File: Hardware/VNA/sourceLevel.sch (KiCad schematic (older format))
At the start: 23 parts, among them U5 AD8319, U6 PE43711, U7 TRF37A75

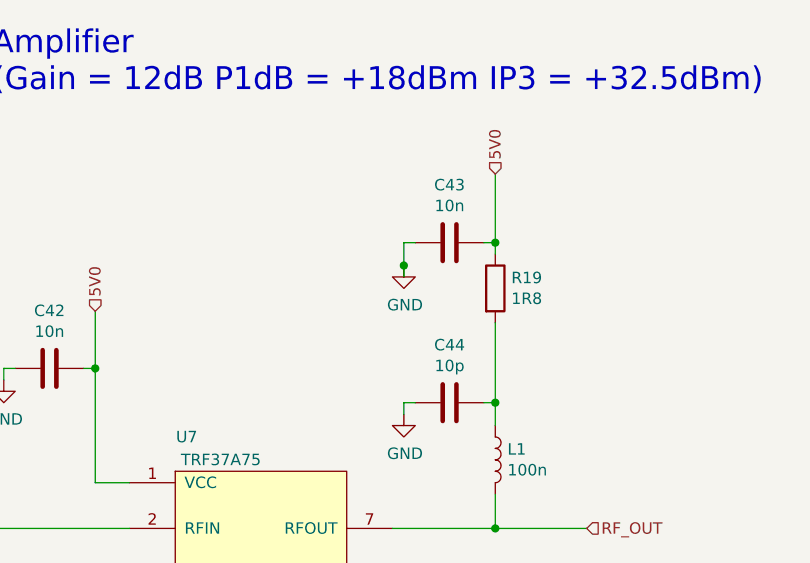
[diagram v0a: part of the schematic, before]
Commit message: added footprints and 3d models
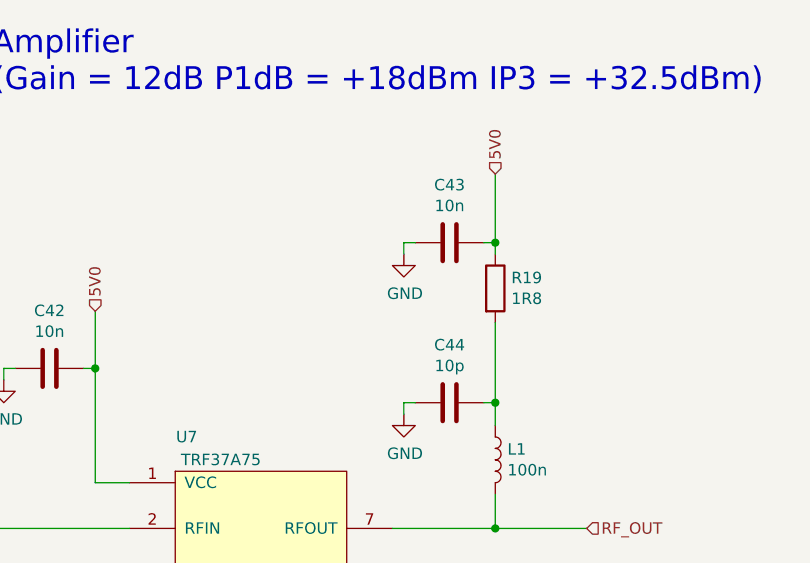
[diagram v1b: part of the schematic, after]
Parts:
- R17, R18: footprint (none) -> Resistor_SMD:R_0603_1608Metric
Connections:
- wire segments 110 -> 109
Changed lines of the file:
@@
 Connection ~ 6500 3800
 $Comp
-L power:GND #PWR045
+L power:GND #PWR044
 U 1 1 5C86EFC4
 P 6800 3850
-F 0 "#PWR045" H 6800 3600 50  0001 C CNN
+F 0 "#PWR044" H 6800 3600 50  0001 C CNN
 F 1 "GND" H 6805 3677 50  0000 C CNN
 F 2 "" H 6800 3850 50  0001 C CNN
@@
 F 0 "R17" H 5470 3446 50  0000 L CNN
 F 1 "0R" H 5470 3355 50  0000 L CNN
-F 2 "" V 5330 3400 50  0001 C CNN
+F 2 "Resistor_SMD:R_0603_1608Metric" V 5330 3400 50  0001 C CNN
 F 3 "~" H 5400 3400 50  0001 C CNN
 	1    5400 3400
@@
 F 0 "R18" H 5470 3846 50  0000 L CNN
 F 1 "DNP" H 5470 3755 50  0000 L CNN
-F 2 "" V 5330 3800 50  0001 C CNN
+F 2 "Resistor_SMD:R_0603_1608Metric" V 5330 3800 50  0001 C CNN
 F 3 "~" H 5400 3800 50  0001 C CNN
 	1    5400 3800
@@
 	5400 3250 5400 3200
 $Comp
-L power:GND #PWR043
+L power:GND #PWR042
 U 1 1 5CB1FC94
 P 5400 4000
-F 0 "#PWR043" H 5400 3750 50  0001 C CNN
+F 0 "#PWR042" H 5400 3750 50  0001 C CNN
 F 1 "GND" H 5405 3827 50  0000 C CNN
 F 2 "" H 5400 4000 50  0001 C CNN
@@
 	7600 1350 7600 1650
 $Comp
+L power:GND #PWR045
+U 1 1 5C8784A2
+P 7200 1700
+F 0 "#PWR045" H 7200 1450 50  0001 C CNN
+F 1 "GND" H 7205 1527 50  0000 C CNN
+F 2 "" H 7200 1700 50  0001 C CNN
+F 3 "" H 7200 1700 50  0001 C CNN
+	1    7200 1700
+	1    0    0    -1
+$EndComp
+$Comp
 L power:GND #PWR046
-U 1 1 5C8784A2
-P 7200 1750
-F 0 "#PWR046" H 7200 1500 50  0001 C CNN
-F 1 "GND" H 7205 1577 50  0000 C CNN
-F 2 "" H 7200 1750 50  0001 C CNN
-F 3 "" H 7200 1750 50  0001 C CNN
-	1    7200 1750
-	1    0    0    -1
-$EndComp
-$Comp
-L power:GND #PWR047
 U 1 1 5C87587D
 P 7200 2400
-F 0 "#PWR047" H 7200 2150 50  0001 C CNN
+F 0 "#PWR046" H 7200 2150 50  0001 C CNN
 F 1 "GND" H 7205 2227 50  0000 C CNN
 F 2 "" H 7200 2400 50  0001 C CNN
@@
 $EndComp
 Wire Wire Line
-	7200 1650 7200 1750
-Wire Wire Line
 	5450 2200 5450 2250
 $Comp
-L power:GND #PWR044
+L power:GND #PWR043
 U 1 1 5CCF0441
 P 5450 2250
-F 0 "#PWR044" H 5450 2000 50  0001 C CNN
+F 0 "#PWR043" H 5450 2000 50  0001 C CNN
 F 1 "GND" H 5455 2077 50  0000 C CNN
 F 2 "" H 5450 2250 50  0001 C CNN
@@
 Wire Wire Line
 	5150 5700 5150 5750
-Connection ~ 7200 1750
-Wire Wire Line
-	7200 1750 7200 1800
 Text HLabel 2450 5200 0    50   Input ~ 0
 RF_PWR_IN
@@
 	7250 3200 7150 3200
 $Comp
-L power:GND #PWR048
+L power:GND #PWR047
 U 1 1 5C86ED9F
 P 7250 3300
-F 0 "#PWR048" H 7250 3050 50  0001 C CNN
+F 0 "#PWR047" H 7250 3050 50  0001 C CNN
 F 1 "GND" H 7255 3127 50  0000 C CNN
 F 2 "" H 7250 3300 50  0001 C CNN
@@
 Text HLabel 5400 3200 1    50   Input ~ 0
 3V3A
+Wire Wire Line
+	7200 1650 7200 1700
 $EndSCHEMATC

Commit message: prelim schematic capture complete
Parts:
- renumbered C34 to C36, C35 to C37, C36 to C38, C37 to C39, C38 to C40, C39 to C41, C40 to C42, C41 to C43, C42 to C44, C43 to C45, C44 to C46, R12 to R19, R13 to R20, R14 to R21, R15 to R22, R16 to R23, R17 to R24, R18 to R25, R19 to R26, U5 to U7, U6 to U8, U7 to U9

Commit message: all 3d models created, prelim bom generated
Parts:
- added TP16: TP, TestPoint:TestPoint_Pad_D1.0mm, symbol Connector:TestPoint
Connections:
- wire segments 109 -> 114
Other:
- moved on the sheet: C38, C39
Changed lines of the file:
@@
 	1    0    0    -1
 $EndComp
-Text Label 4700 3350 2    50   ~ 6
+Text Label 4700 3350 2    50   ~ 0
 nP_S
-Text Label 4700 3500 2    50   ~ 6
-SI
-Text Label 4700 3700 2    50   ~ 6
-LE
-Text Label 4700 3600 2    50   ~ 6
-CLK
 Wire Wire Line
 	4400 3500 4700 3500
@@
 L Device:C C39
 U 1 1 5CC58ACB
-P 3750 2300
-F 0 "C39" V 3700 2200 50  0000 C CNN
-F 1 "100p" V 3900 2300 50  0000 C CNN
-F 2 "Capacitor_SMD:C_0402_1005Metric" H 3788 2150 50  0001 C CNN
-F 3 "~" H 3750 2300 50  0001 C CNN
-	1    3750 2300
+P 3900 2300
+F 0 "C39" V 3850 2150 50  0000 C CNN
+F 1 "100p" V 4050 2300 50  0000 C CNN
+F 2 "Capacitor_SMD:C_0402_1005Metric" H 3938 2150 50  0001 C CNN
+F 3 "~" H 3900 2300 50  0001 C CNN
+	1    3900 2300
 	0    1    1    0
 $EndComp
@@
 L Device:C C38
 U 1 1 5C364B92
-P 3750 1950
-F 0 "C38" V 3700 1850 50  0000 C CNN
-F 1 "100n" V 3900 1950 50  0000 C CNN
-F 2 "Capacitor_SMD:C_0402_1005Metric" H 3788 1800 50  0001 C CNN
-F 3 "~" H 3750 1950 50  0001 C CNN
-	1    3750 1950
-	0    1    1    0
-$EndComp
-Wire Wire Line
-	3600 1750 3600 1950
+P 3900 1950
+F 0 "C38" V 3850 1800 50  0000 C CNN
+F 1 "100n" V 4050 1950 50  0000 C CNN
+F 2 "Capacitor_SMD:C_0402_1005Metric" H 3938 1800 50  0001 C CNN
+F 3 "~" H 3900 1950 50  0001 C CNN
+	1    3900 1950
+	0    1    1    0
+$EndComp
 $Comp
 L power:GND #PWR058
 U 1 1 5C36FE30
-P 3900 2400
-F 0 "#PWR058" H 3900 2150 50  0001 C CNN
-F 1 "GND" H 3905 2227 50  0000 C CNN
-F 2 "" H 3900 2400 50  0001 C CNN
-F 3 "" H 3900 2400 50  0001 C CNN
-	1    3900 2400
-	1    0    0    -1
-$EndComp
-Connection ~ 3600 1950
-Wire Wire Line
-	3900 2300 3900 2400
-Connection ~ 3600 2300
-Wire Wire Line
-	3600 1950 3600 2300
-Wire Wire Line
-	3900 1950 3900 2300
-Connection ~ 3900 2300
-Wire Wire Line
-	3600 2300 3600 2550
-Text Notes 2750 850  0    100  ~ 6
+P 4050 2400
+F 0 "#PWR058" H 4050 2150 50  0001 C CNN
+F 1 "GND" H 4055 2227 50  0000 C CNN
+F 2 "" H 4050 2400 50  0001 C CNN
+F 3 "" H 4050 2400 50  0001 C CNN
+	1    4050 2400
+	1    0    0    -1
+$EndComp
+Wire Wire Line
+	4050 2300 4050 2400
+Wire Wire Line
+	4050 1950 4050 2300
+Connection ~ 4050 2300
+Text Notes 2750 850  0    100  ~ 0
 Programmable Attenuator
 Wire Wire Line
@@
 Wire Wire Line
 	5400 3600 5400 3650
-Text HLabel 2500 2900 0    50   Input ~ 6
+Text HLabel 2500 2900 0    50   Input ~ 0
 RF_IN
-Text HLabel 8000 2900 2    50   Input ~ 6
+Text HLabel 8000 2900 2    50   Input ~ 0
 RF_OUT
-Text HLabel 4700 3500 2    50   Input ~ 6
+Text HLabel 4700 3500 2    50   Input ~ 0
 SI
 Wire Wire Line
@@
 Connection ~ 4350 6100
 Wire Wire Line
-	4850 6100 5250 6100
-Text Notes 2900 4900 0    100  ~ 6
+	4850 6100 5050 6100
+Text Notes 2900 4900 0    100  ~ 0
 Power Detector\n
 $Comp
@@
 Wire Wire Line
 	5000 5700 5150 5700
-Text HLabel 4700 3600 2    50   Input ~ 6
+Text HLabel 4700 3600 2    50   Input ~ 0
 CLK
-Text HLabel 4700 3700 2    50   Input ~ 6
+Text HLabel 4700 3700 2    50   Input ~ 0
 LE
-Text Notes 5400 1000 0    100  ~ 6
+Text Notes 5400 1000 0    100  ~ 0
 Amplifier \n(Gain = 12dB P1dB = +18dBm IP3 = +32.5dBm)
 Wire Wire Line
@@
 Wire Wire Line
 	5150 5700 5150 5750
-Text HLabel 2450 5200 0    50   Input ~ 6
+Text HLabel 2450 5200 0    50   Input ~ 0
 RF_PWR_IN
-Text HLabel 5250 6100 2    50   Output ~ 6
+Text HLabel 5250 6100 2    50   Output ~ 0
 PWR_LEVEL
-Text HLabel 3600 1750 1    50   Input ~ 6
+Text HLabel 3600 1750 1    50   Input ~ 0
 3V3A
-Text HLabel 5850 1950 1    50   Input ~ 6
+Text HLabel 5850 1950 1    50   Input ~ 0
 5V0
-Text HLabel 7600 1350 1    50   Input ~ 6
+Text HLabel 7600 1350 1    50   Input ~ 0
 5V0
 Wire Wire Line
@@
 Wire Wire Line
 	7250 3300 7250 3200
-Text HLabel 6000 3200 0    50   Input ~ 6
+Text HLabel 6000 3200 0    50   Input ~ 0
 PWRDN
-Text HLabel 4650 5350 1    50   Input ~ 6
+Text HLabel 4650 5350 1    50   Input ~ 0
 3V3A
-Text HLabel 5400 3200 1    50   Input ~ 6
+Text HLabel 5400 3200 1    50   Input ~ 0
 3V3A
 Wire Wire Line
 	7200 1650 7200 1700
+$Comp
+L Connector:TestPoint TP16
+U 1 1 5CECA150
+P 5150 6300
+F 0 "TP16" V 5104 6488 50  0000 L CNN
+F 1 "TP" V 5195 6488 50  0000 L CNN
+F 2 "TestPoint:TestPoint_Pad_D1.0mm" H 5350 6300 50  0001 C CNN
+F 3 "~" H 5350 6300 50  0001 C CNN
+	1    5150 6300
+	0    1    1    0
+$EndComp
+Wire Wire Line
+	5150 6300 5050 6300
+Wire Wire Line
+	5050 6300 5050 6100
+Connection ~ 5050 6100
+Wire Wire Line
+	5050 6100 5250 6100
+Wire Wire Line
+	3600 1750 3600 1950
+Wire Wire Line
+	3750 2300 3600 2300
+Connection ~ 3600 2300
+Wire Wire Line
+	3600 2300 3600 2550
+Wire Wire Line
+	3750 1950 3600 1950
+Connection ~ 3600 1950
+Wire Wire Line
+	3600 1950 3600 2300
 $EndSCHEMATC

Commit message: More schematic changes + updated functionals
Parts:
- removed U8: PE43711, VNA_Footprints:QFN-24-1EP_4x4mm_P0.5mm_EP2.7x2.6mm_ThermalVias, symbol VNA_Symbols:PE43711
- added U8: SKY12347-362LF, Package_DFN_QFN:QFN-24-1EP_4x4mm_P0.5mm_EP2.7x2.7mm_ThermalVias, symbol VNA_Symbols:SKY12347-362LF
- R24: value 0R -> 0R0
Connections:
- net labels added: SDI, SDO
- net labels removed: SI, nP_S
- no-connect marks 7 -> 6
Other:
- note added: "Sets init state \nto full attenuation"
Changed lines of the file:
@@
 Comment4 ""
 $EndDescr
-$Comp
-L VNA_Symbols:PE43711 U8
-U 1 1 5CC58AC9
-P 3600 3350
-F 0 "U8" H 3050 4100 50  0000 C CNN
-F 1 "PE43711" H 3150 4000 50  0000 C CNN
-F 2 "VNA_Footprints:QFN-24-1EP_4x4mm_P0.5mm_EP2.7x2.6mm_ThermalVias" H 3650 4000 50  0001 C CNN
-F 3 "" H 3650 4000 50  0001 C CNN
-	1    3600 3350
-	1    0    0    -1
-$EndComp
-Text Label 4700 3350 2    50   ~ 0
-nP_S
-Wire Wire Line
-	4400 3500 4700 3500
-Wire Wire Line
-	4400 3700 4700 3700
-Wire Wire Line
-	4400 3600 4700 3600
-Wire Wire Line
-	4100 4300 4100 4250
-Wire Wire Line
-	4000 4250 4000 4300
-Connection ~ 4000 4300
-Wire Wire Line
-	4000 4300 4100 4300
 Wire Wire Line
 	3900 4250 3900 4300
 Connection ~ 3900 4300
-Wire Wire Line
-	3900 4300 4000 4300
 $Comp
 L power:GND #PWR059
 U 1 1 5C364909
-P 4100 4300
-F 0 "#PWR059" H 4100 4050 50  0001 C CNN
-F 1 "GND" H 4105 4127 50  0000 C CNN
-F 2 "" H 4100 4300 50  0001 C CNN
-F 3 "" H 4100 4300 50  0001 C CNN
-	1    4100 4300
-	1    0    0    -1
-$EndComp
-Connection ~ 4100 4300
+P 3900 4350
+F 0 "#PWR059" H 3900 4100 50  0001 C CNN
+F 1 "GND" H 3905 4177 50  0000 C CNN
+F 2 "" H 3900 4350 50  0001 C CNN
+F 3 "" H 3900 4350 50  0001 C CNN
+	1    3900 4350
+	1    0    0    -1
+$EndComp
 $Comp
 L Device:C C39
@@
 	4050 1950 4050 2300
 Connection ~ 4050 2300
-Text Notes 2750 850  0    100  ~ 0
+Text Notes 2750 850  0    100  ~ 6
 Programmable Attenuator
 Wire Wire Line
@@
 $EndComp
 Wire Wire Line
-	3100 4250 3100 4300
-Wire Wire Line
-	3100 4300 3200 4300
-Wire Wire Line
 	3800 4250 3800 4300
 Connection ~ 3800 4300
@@
 Wire Wire Line
 	3200 4250 3200 4300
-Connection ~ 3200 4300
 Wire Wire Line
 	3200 4300 3300 4300
 Wire Wire Line
 	4400 2900 5000 2900
-NoConn ~ 2800 3100
-NoConn ~ 2800 3200
-NoConn ~ 2800 3300
-NoConn ~ 2800 3400
-NoConn ~ 2800 3500
-NoConn ~ 2800 3600
-NoConn ~ 2800 3700
-$Comp
-L Device:R R24
-U 1 1 5CB195A2
-P 5400 3400
-F 0 "R24" H 5470 3446 50  0000 L CNN
-F 1 "0R" H 5470 3355 50  0000 L CNN
-F 2 "Resistor_SMD:R_0603_1608Metric" V 5330 3400 50  0001 C CNN
-F 3 "~" H 5400 3400 50  0001 C CNN
-	1    5400 3400
-	1    0    0    -1
-$EndComp
-$Comp
-L Device:R R25
-U 1 1 5CB19A2E
-P 5400 3800
-F 0 "R25" H 5470 3846 50  0000 L CNN
-F 1 "DNP" H 5470 3755 50  0000 L CNN
-F 2 "Resistor_SMD:R_0603_1608Metric" V 5330 3800 50  0001 C CNN
-F 3 "~" H 5400 3800 50  0001 C CNN
-	1    5400 3800
-	1    0    0    -1
-$EndComp
-Wire Wire Line
-	4400 3350 5200 3350
-Wire Wire Line
-	5400 3950 5400 4000
-Wire Wire Line
-	5400 3250 5400 3200
-$Comp
-L power:GND #PWR063
-U 1 1 5CB1FC94
-P 5400 4000
-F 0 "#PWR063" H 5400 3750 50  0001 C CNN
-F 1 "GND" H 5405 3827 50  0000 C CNN
-F 2 "" H 5400 4000 50  0001 C CNN
-F 3 "" H 5400 4000 50  0001 C CNN
-	1    5400 4000
-	1    0    0    -1
-$EndComp
-Wire Wire Line
-	5400 3550 5400 3600
-Wire Wire Line
-	5200 3600 5400 3600
-Wire Wire Line
-	5200 3350 5200 3600
-Connection ~ 5400 3600
-Wire Wire Line
-	5400 3600 5400 3650
-Text HLabel 2500 2900 0    50   Input ~ 0
+Text HLabel 2500 2900 0    50   Input ~ 6
 RF_IN
-Text HLabel 8000 2900 2    50   Input ~ 0
+Text HLabel 8000 2900 2    50   Input ~ 6
 RF_OUT
-Text HLabel 4700 3500 2    50   Input ~ 0
-SI
 Wire Wire Line
 	4450 5200 4450 5300
@@
 Wire Wire Line
 	4850 6100 5050 6100
-Text Notes 2900 4900 0    100  ~ 0
+Text Notes 2900 4900 0    100  ~ 6
 Power Detector\n
 $Comp
@@
 Wire Wire Line
 	5000 5700 5150 5700
-Text HLabel 4700 3600 2    50   Input ~ 0
-CLK
-Text HLabel 4700 3700 2    50   Input ~ 0
-LE
-Text Notes 5400 1000 0    100  ~ 0
+Text Notes 5400 1000 0    100  ~ 6
 Amplifier \n(Gain = 12dB P1dB = +18dBm IP3 = +32.5dBm)
 Wire Wire Line
@@
 Wire Wire Line
 	5150 5700 5150 5750
-Text HLabel 2450 5200 0    50   Input ~ 0
+Text HLabel 2450 5200 0    50   Input ~ 6
 RF_PWR_IN
-Text HLabel 5250 6100 2    50   Output ~ 0
+Text HLabel 5250 6100 2    50   Output ~ 6
 PWR_LEVEL
-Text HLabel 3600 1750 1    50   Input ~ 0
+Text HLabel 3600 1750 1    50   Input ~ 6
 3V3A
-Text HLabel 5850 1950 1    50   Input ~ 0
+Text HLabel 5850 1950 1    50   Input ~ 6
 5V0
-Text HLabel 7600 1350 1    50   Input ~ 0
+Text HLabel 7600 1350 1    50   Input ~ 6
 5V0
 Wire Wire Line
@@
 Wire Wire Line
 	7250 3300 7250 3200
-Text HLabel 6000 3200 0    50   Input ~ 0
+Text HLabel 6000 3200 0    50   Input ~ 6
 PWRDN
-Text HLabel 4650 5350 1    50   Input ~ 0
-3V3A
-Text HLabel 5400 3200 1    50   Input ~ 0
+Text HLabel 4650 5350 1    50   Input ~ 6
 3V3A
 Wire Wire Line
@@
 Wire Wire Line
 	3600 1950 3600 2300
+$Comp
+L VNA_Symbols:SKY12347-362LF U8
+U 1 1 5CB0A6D7
+P 3600 3350
+F 0 "U8" H 3050 4100 50  0000 C CNN
+F 1 "SKY12347-362LF" H 3200 4000 50  0000 C CNN
+F 2 "Package_DFN_QFN:QFN-24-1EP_4x4mm_P0.5mm_EP2.7x2.7mm_ThermalVias" H 3650 4000 50  0001 C CNN
+F 3 "" H 3650 4000 50  0001 C CNN
+	1    3600 3350
+	1    0    0    -1
+$EndComp
+Wire Wire Line
+	2800 3250 2750 3250
+Wire Wire Line
+	2800 3450 2750 3450
+Wire Wire Line
+	2800 3150 2750 3150
+$Comp
+L Device:R R24
+U 1 1 5CB0F084
+P 2350 3600
+F 0 "R24" H 2420 3646 50  0000 L CNN
+F 1 "0R0" H 2420 3555 50  0000 L CNN
+F 2 "Resistor_SMD:R_0603_1608Metric" V 2280 3600 50  0001 C CNN
+F 3 "~" H 2350 3600 50  0001 C CNN
+	1    2350 3600
+	-1   0    0    -1
+$EndComp
+$Comp
+L Device:R R25
+U 1 1 5CB0F08A
+P 2350 4000
+F 0 "R25" H 2420 4046 50  0000 L CNN
+F 1 "DNP" H 2420 3955 50  0000 L CNN
+F 2 "Resistor_SMD:R_0603_1608Metric" V 2280 4000 50  0001 C CNN
+F 3 "~" H 2350 4000 50  0001 C CNN
+	1    2350 4000
+	-1   0    0    -1
+$EndComp
+Wire Wire Line
+	2800 3550 2550 3550
+Wire Wire Line
+	2350 4150 2350 4200
+Wire Wire Line
+	2350 3450 2350 3400
+$Comp
+L power:GND #PWR063
+U 1 1 5CB0F093
+P 2350 4200
+F 0 "#PWR063" H 2350 3950 50  0001 C CNN
+F 1 "GND" H 2355 4027 50  0000 C CNN
+F 2 "" H 2350 4200 50  0001 C CNN
+F 3 "" H 2350 4200 50  0001 C CNN
+	1    2350 4200
+	-1   0    0    -1
+$EndComp
+Wire Wire Line
+	2350 3750 2350 3800
+Wire Wire Line
+	2550 3800 2350 3800
+Wire Wire Line
+	2550 3550 2550 3800
+Connection ~ 2350 3800
+Wire Wire Line
+	2350 3800 2350 3850
+Text HLabel 2750 3250 0    50   Input ~ 6
+SDI
+Text HLabel 2750 3150 0    50   Input ~ 6
+CLK
+Text HLabel 2750 3450 0    50   Input ~ 6
+LE
+Text HLabel 2350 3400 1    50   Input ~ 6
+3V3A
+Wire Wire Line
+	3900 4300 3900 4350
+NoConn ~ 4400 3400
+NoConn ~ 4400 3500
+NoConn ~ 4400 3600
+NoConn ~ 4400 3700
+NoConn ~ 4400 3800
+NoConn ~ 4400 3900
+Wire Wire Line
+	2800 3350 2750 3350
+Text HLabel 2750 3350 0    50   Input ~ 6
+SDO
+Wire Wire Line
+	4400 3150 4550 3150
+Wire Wire Line
+	4550 3150 4550 3250
+Wire Wire Line
+	4400 3250 4550 3250
+Wire Wire Line
+	4550 3250 4550 3300
+Connection ~ 4550 3250
+$Comp
+L power:GND #PWR0122
+U 1 1 5CB3AAC5
+P 4550 3300
+F 0 "#PWR0122" H 4550 3050 50  0001 C CNN
+F 1 "GND" H 4555 3127 50  0000 C CNN
+F 2 "" H 4550 3300 50  0001 C CNN
+F 3 "" H 4550 3300 50  0001 C CNN
+	1    4550 3300
+	1    0    0    -1
+$EndComp
+Text Notes 4600 3300 0    50   ~ 6
+Sets init state \nto full attenuation
 $EndSCHEMATC

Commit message: first day of layout / routing done
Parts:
- added D18: LED, LED_SMD:LED_0603_1608Metric, symbol Device:LED
- added R63: 470R, Resistor_SMD:R_0603_1608Metric, symbol Device:R
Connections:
- wire segments 114 -> 120
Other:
- note added: "PA ON"
